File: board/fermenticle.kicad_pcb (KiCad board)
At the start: 2 copper layers, 78 x 43 mm, 28 parts, among them IC1 DS2482-100S, J1 1Wire, J3 POWER, P1 DISPLAY, P2 DO0, P6 SD Card, P7 DO 1-3, U1 74hct125d, U2 7805, U3 PHOTON

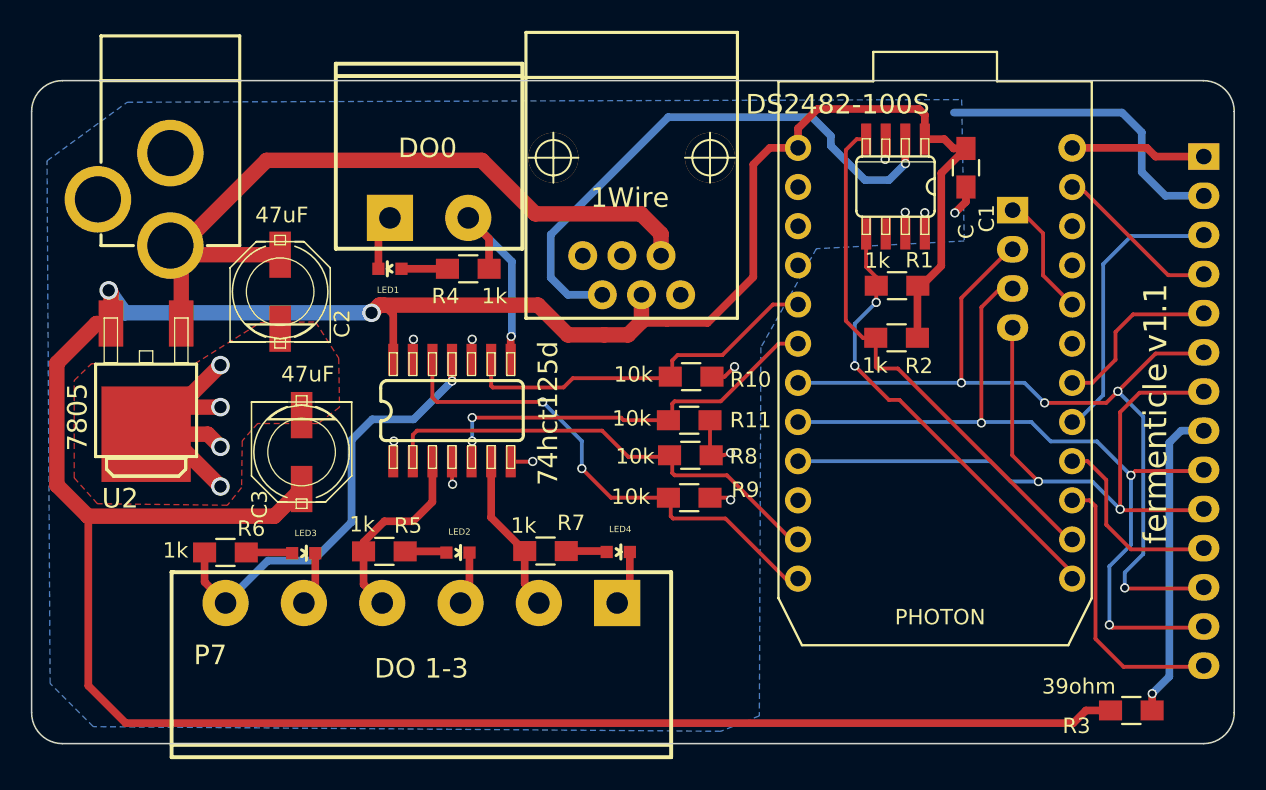
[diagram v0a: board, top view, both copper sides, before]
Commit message: Better layout for v1.1
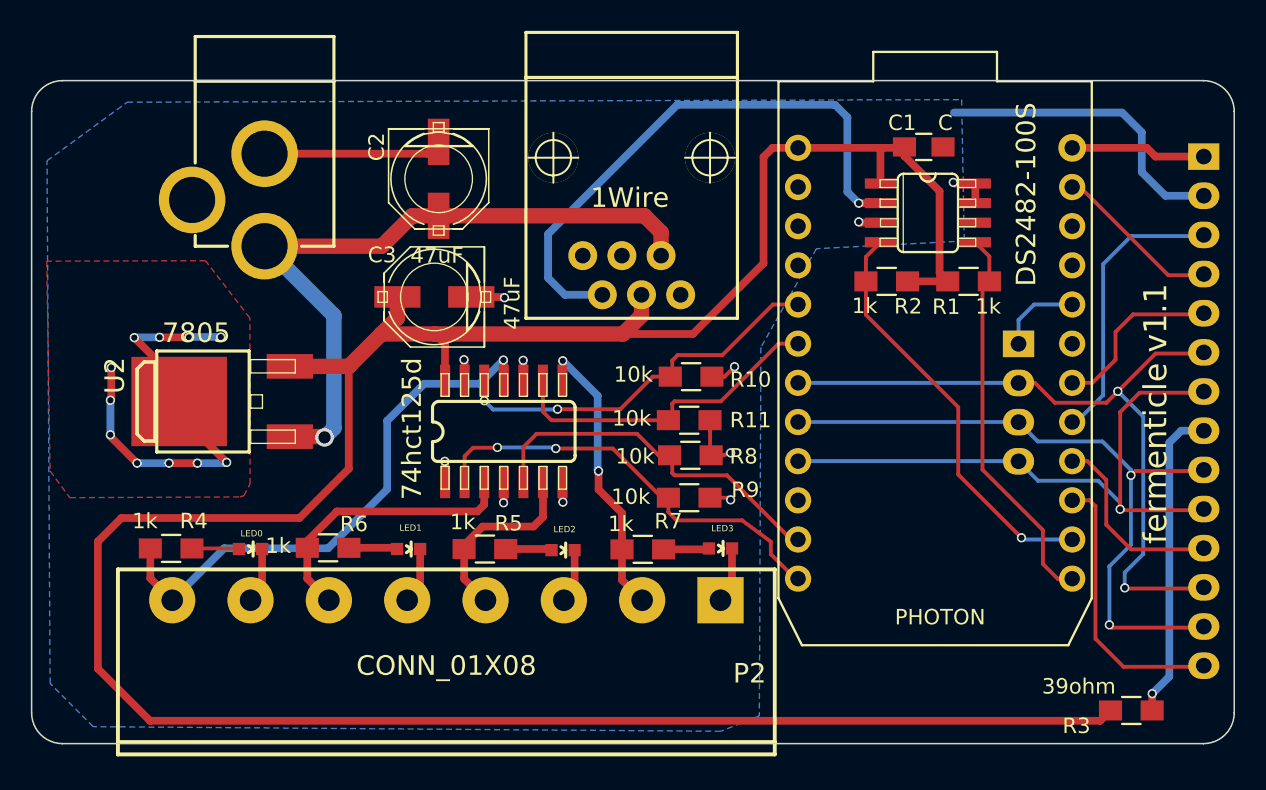
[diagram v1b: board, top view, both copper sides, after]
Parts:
- removed LED4: LED, SparkFun:SparkFun-LED-0603
- removed P7: DO 1-3, w_conn_screw:mstba_2,5%2f6-g-5,08
- added LED0: LED, SparkFun:SparkFun-LED-0603, F.Cu at (133.2, 126.4)
- P2: value DO0 -> CONN_01X08; footprint w_conn_screw:mstba_2,5%2f2-g-5,08 -> w_conn_screw:mstba_2,5%2f8-g-5,08
- moved LED3 27.0 mm to (163.7, 126.3)
- moved R4 26.5 mm to (128.1, 126.3), turned to 0 degrees
- moved P2 24.8 mm to (145.9, 129.7), turned to 180 degrees
- moved LED1 18.2 mm to (143.4, 126.4), turned to 270 degrees
- moved C3 13.2 mm to (145.1, 110.0), turned to 180 degrees
- moved C2 12.6 mm to (145.4, 102.4), turned to 270 degrees
- moved P6 8.68 mm to (183.0, 113.1)
- moved LED2 6.82 mm to (153.5, 126.5)
- moved R6 6.67 mm to (138.2, 126.3)
- moved R5 6.52 mm to (148.4, 126.4)
- moved R7 6.31 mm to (158.6, 126.4)
- moved J3 6.11 mm to (134.1, 93.0)
- moved R1 4.65 mm to (179.8, 109.0), turned to 0 degrees
- moved U2 4.53 mm to (130.9, 116.8), turned to 90 degrees
- moved R2 3.72 mm to (174.5, 109.0)
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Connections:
- P2 pad 2: ACT0_5V -> ACT3_5V
- R4 pad 2: Net-(LED1-PadA) -> Net-(LED0-PadA)
- R6 pad 2: Net-(LED3-PadA) -> Net-(LED1-PadA)
- R7 pad 2: Net-(LED4-PadA) -> Net-(LED3-PadA)
- U1 pad 11: ACT1_5V -> ACT0_5V
- U1 pad 12: ACT1 -> ACT0
- U1 pad 2: ACT2 -> ACT1
- U1 pad 3: ACT2_5V -> ACT1_5V
- U1 pad 5: ACT3 -> ACT2
- U1 pad 6: ACT3_5V -> ACT2_5V
- U1 pad 8: ACT0_5V -> ACT3_5V
- U1 pad 9: ACT0 -> ACT3
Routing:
- net +5V: track 202.5 -> 175.4 mm, vias 2 -> 0
- net ACT0_5V: track 15.2 -> 35.8 mm
- net GND: track 82.0 -> 94.8 mm, vias 16 -> 22
- net ACT1_5V: track 29.0 -> 18.3 mm, vias 1 -> 0
- net SCK: track 50.7 -> 40.1 mm, vias 2 -> 1
- net MOSI: track 57.4 -> 47.2 mm, vias 4 -> 2
- net MISO: track 54.4 -> 44.5 mm, vias 3 -> 2
- net ACT3_5V: track 10.8 -> 18.9 mm, vias 0 -> 2
- net SCL: track 34.3 -> 27.1 mm, vias 0 -> 1
- net +12V: track 52.0 -> 45.3 mm, vias 0 -> 1
- net ACT2: track 30.4 -> 23.7 mm
- net ACT3: track 26.4 -> 21.1 mm, vias 2 -> 0
- net ACT1: track 32.8 -> 28.0 mm
- net SDA: track 29.4 -> 25.3 mm, vias 2 -> 0
- net Net-(LED0-PadA): track 0.00 -> 3.07 mm
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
